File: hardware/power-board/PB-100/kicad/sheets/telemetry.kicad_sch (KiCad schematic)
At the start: 0 parts

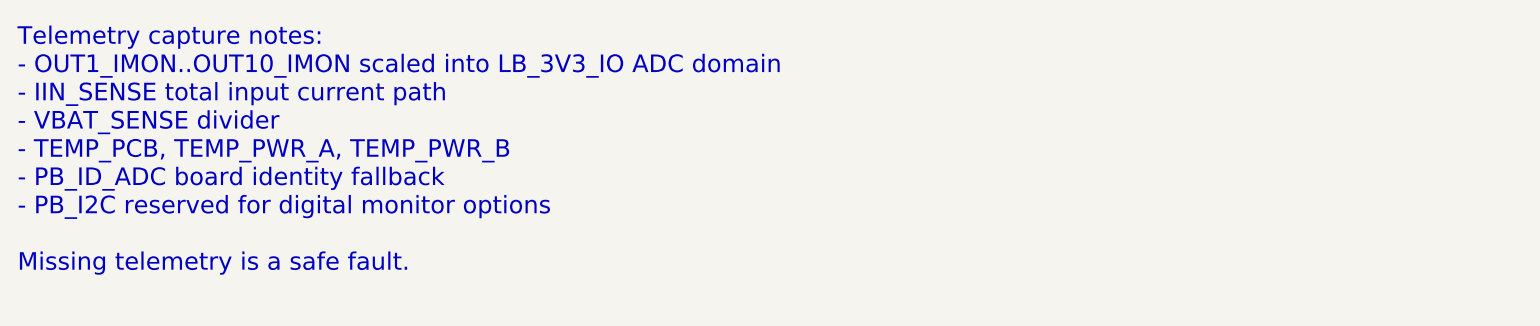
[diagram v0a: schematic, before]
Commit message: hardware: sync pb100 kicad sheet trace notes
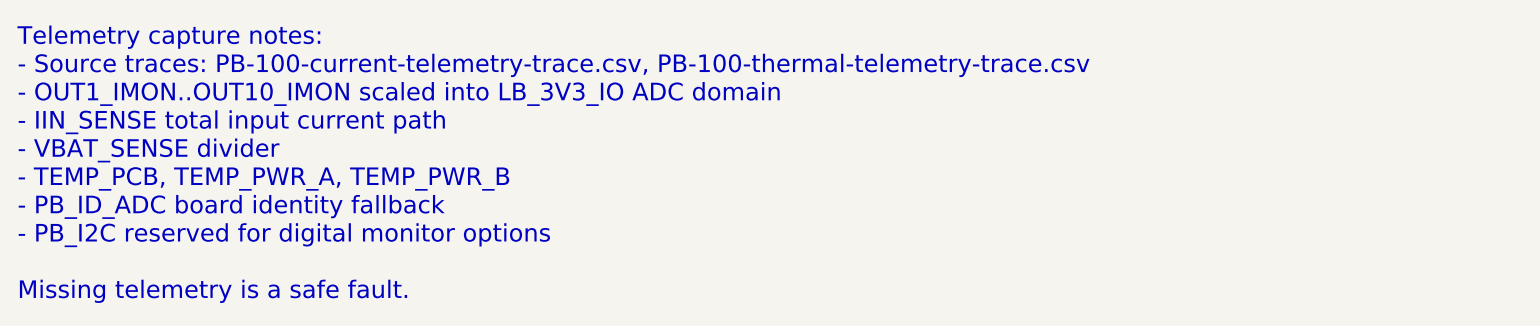
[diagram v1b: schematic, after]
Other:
- note added: "Telemetry capture notes: - Source traces: PB-100-current-telemetry-trace.csv, PB-100-thermal-telemetry-trace.csv - OUT1_IMON..OUT10_IMON scaled into LB_3V3_IO ADC domain - IIN_SENSE total input current path - VBAT_SENSE divider - TEMP_PCB, TEMP_PWR_A, TEMP_PWR_B - PB_ID_ADC board identity fallback - PB_I2C reserved for digital monitor options Missing telemetry is a safe fault."
- note removed: "Telemetry capture notes: - OUT1_IMON..OUT10_IMON scaled into LB_3V3_IO ADC domain - IIN_SENSE total input current path - VBAT_SENSE divider - TEMP_PCB, TEMP_PWR_A, TEMP_PWR_B - PB_ID_ADC board identity fallback - PB_I2C reserved for digital monitor options Missing telemetry is a safe fault."
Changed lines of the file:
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@@
     (comment 9 "Work queue: CAP-TEL. Telemetry capture follows current and thermal maps.")
     (comment 1 "Placeholder sheet. Capture current, voltage, thermal, and board ID telemetry here.")
-    (comment 2 "Sources: PB-100-current-telemetry.md and PB-100-thermal-telemetry.md.")
+    (comment 2 "Sources: PB-100-current-telemetry-trace.csv, PB-100-thermal-telemetry-trace.csv, telemetry maps.")
   )
-  (text "Telemetry capture notes:\n- OUT1_IMON..OUT10_IMON scaled into LB_3V3_IO ADC domain\n- IIN_SENSE total input current path\n- VBAT_SENSE divider\n- TEMP_PCB, TEMP_PWR_A, TEMP_PWR_B\n- PB_ID_ADC board identity fallback\n- PB_I2C reserved for digital monitor options\n\nMissing telemetry is a safe fault."
+  (text "Telemetry capture notes:\n- Source traces: PB-100-current-telemetry-trace.csv, PB-100-thermal-telemetry-trace.csv\n- OUT1_IMON..OUT10_IMON scaled into LB_3V3_IO ADC domain\n- IIN_SENSE total input current path\n- VBAT_SENSE divider\n- TEMP_PCB, TEMP_PWR_A, TEMP_PWR_B\n- PB_ID_ADC board identity fallback\n- PB_I2C reserved for digital monitor options\n\nMissing telemetry is a safe fault."
     (at 25 30 0)
     (effects (font (size 2.0 2.0)) (justify left top))

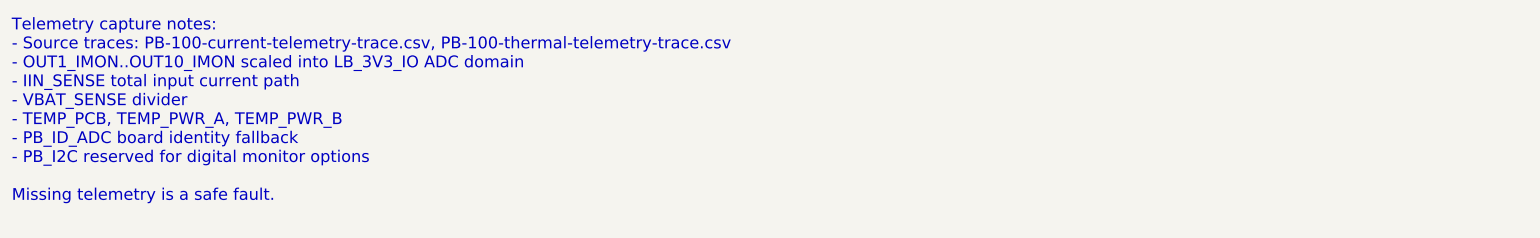
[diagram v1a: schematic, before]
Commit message: hardware: add pb100 current telemetry freeze review
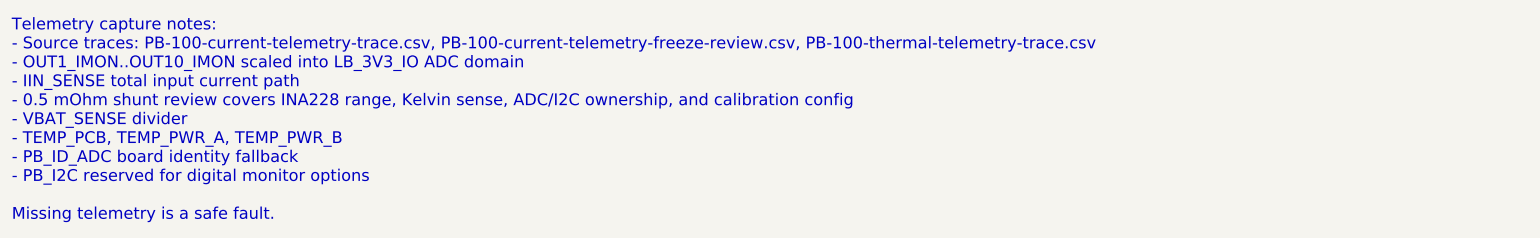
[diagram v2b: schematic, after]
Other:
- note added: "Telemetry capture notes: - Source traces: PB-100-current-telemetry-trace.csv, PB-100-current-telemetry-freeze-review.csv, PB-100-thermal-telemetry-trace.csv - OUT1_IMON..OUT10_IMON scaled into LB_3V3_IO ADC domain - IIN_SENSE total input current path - 0.5 mOhm shunt review covers INA228 range, Kelvin sense, ADC/I2C ownership, and calibration config - VBAT_SENSE divider - TEMP_PCB, TEMP_PWR_A, TE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"
- note removed: "Telemetry capture notes: - Source traces: PB-100-current-telemetry-trace.csv, PB-100-thermal-telemetry-trace.csv - OUT1_IMON..OUT10_IMON scaled into LB_3V3_IO ADC domain - IIN_SENSE total input current path - VBAT_SENSE divider - TEMP_PCB, TEMP_PWR_A, TEMP_PWR_B - PB_ID_ADC board identity fallback - PB_I2C reserved for digital monitor options Missing telemetry is a safe fault."
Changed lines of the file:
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@@
     (comment 9 "Work queue: CAP-TEL. Telemetry capture follows current and thermal maps.")
     (comment 1 "Placeholder sheet. Capture current, voltage, thermal, and board ID telemetry here.")
-    (comment 2 "Sources: PB-100-current-telemetry-trace.csv, PB-100-thermal-telemetry-trace.csv, telemetry maps.")
+    (comment 2 "Sources: PB-100-current-telemetry-trace.csv, PB-100-current-telemetry-freeze-review.csv, PB-100-thermal-telemetry-trace.csv, telemetry maps.")
   )
-  (text "Telemetry capture notes:\n- Source traces: PB-100-current-telemetry-trace.csv, PB-100-thermal-telemetry-trace.csv\n- OUT1_IMON..OUT10_IMON scaled into LB_3V3_IO ADC domain\n- IIN_SENSE total input current path\n- VBAT_SENSE divider\n- TEMP_PCB, TEMP_PWR_A, TEMP_PWR_B\n- PB_ID_ADC board identity fallback\n- PB_I2C reserved for digital monitor options\n\nMissing telemetry is a safe fault."
+  (text "Telemetry capture notes:\n- Source traces: PB-100-current-telemetry-trace.csv, PB-100-current-telemetry-freeze-review.csv, PB-100-thermal-telemetry-trace.csv\n- OUT1_IMON..OUT10_IMON scaled into LB_3V3_IO ADC domain\n- IIN_SENSE total input current path\n- 0.5 mOhm shunt review covers INA228 range, Kelvin sense, ADC/I2C ownership, and calibration config\n- VBAT_SENSE divider\n- TEMP_PCB, TEMP_PWR_A, TEMP_PWR_B\n- PB_ID_ADC board identity fallback\n- PB_I2C reserved for digital monitor options\n\nMissing telemetry is a safe fault."
     (at 25 30 0)
     (effects (font (size 2.0 2.0)) (justify left top))

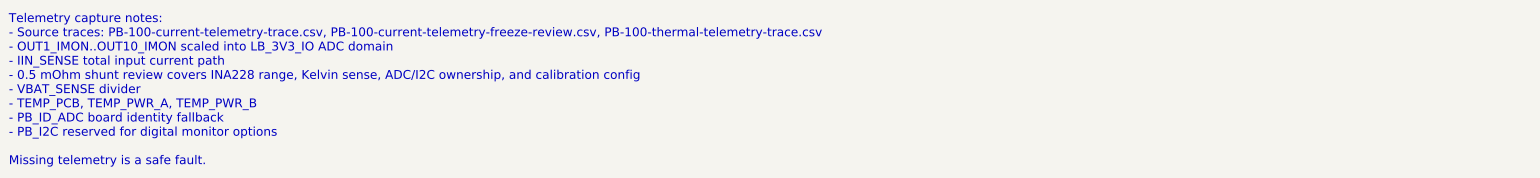
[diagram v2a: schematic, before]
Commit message: hardware: add pb100 thermal telemetry freeze review
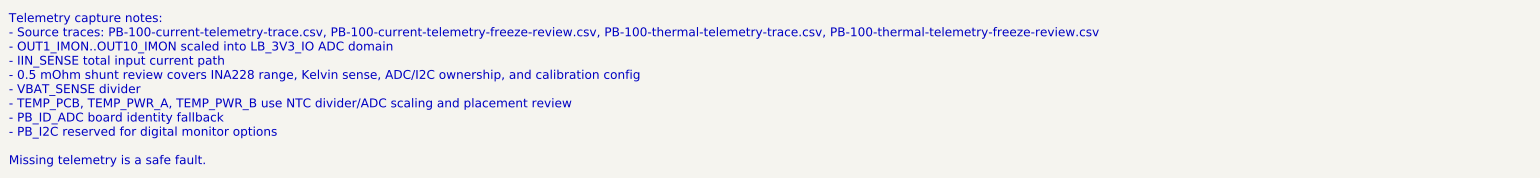
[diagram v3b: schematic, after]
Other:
- note added: "Telemetry capture notes: - Source traces: PB-100-current-telemetry-trace.csv, PB-100-current-telemetry-freeze-review.csv, PB-100-thermal-telemetry-trace.csv, PB-100-thermal-telemetry-freeze-review.csv - OUT1_IMON..OUT10_IMON scaled into LB_3V3_IO ADC domain - IIN_SENSE total input current path - 0.5 mOhm shunt review covers INA228 range, Kelvin sense, ADC/I2C ownership, and calibration config - V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"
- note removed: "Telemetry capture notes: - Source traces: PB-100-current-telemetry-trace.csv, PB-100-current-telemetry-freeze-review.csv, PB-100-thermal-telemetry-trace.csv - OUT1_IMON..OUT10_IMON scaled into LB_3V3_IO ADC domain - IIN_SENSE total input current path - 0.5 mOhm shunt review covers INA228 range, Kelvin sense, ADC/I2C ownership, and calibration config - VBAT_SENSE divider - TEMP_PCB, TEMP_PWR_A, TE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"
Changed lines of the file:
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@@
     (comment 9 "Work queue: CAP-TEL. Telemetry capture follows current and thermal maps.")
     (comment 1 "Placeholder sheet. Capture current, voltage, thermal, and board ID telemetry here.")
-    (comment 2 "Sources: PB-100-current-telemetry-trace.csv, PB-100-current-telemetry-freeze-review.csv, PB-100-thermal-telemetry-trace.csv, telemetry maps.")
+    (comment 2 "Sources: PB-100-current-telemetry-trace.csv, PB-100-current-telemetry-freeze-review.csv, PB-100-thermal-telemetry-trace.csv, PB-100-thermal-telemetry-freeze-review.csv, telemetry maps.")
   )
-  (text "Telemetry capture notes:\n- Source traces: PB-100-current-telemetry-trace.csv, PB-100-current-telemetry-freeze-review.csv, PB-100-thermal-telemetry-trace.csv\n- OUT1_IMON..OUT10_IMON scaled into LB_3V3_IO ADC domain\n- IIN_SENSE total input current path\n- 0.5 mOhm shunt review covers INA228 range, Kelvin sense, ADC/I2C ownership, and calibration config\n- VBAT_SENSE divider\n- TEMP_PCB, TEMP_PWR_A, TEMP_PWR_B\n- PB_ID_ADC board identity fallback\n- PB_I2C reserved for digital monitor options\n\nMissing telemetry is a safe fault."
+  (text "Telemetry capture notes:\n- Source traces: PB-100-current-telemetry-trace.csv, PB-100-current-telemetry-freeze-review.csv, PB-100-thermal-telemetry-trace.csv, PB-100-thermal-telemetry-freeze-review.csv\n- OUT1_IMON..OUT10_IMON scaled into LB_3V3_IO ADC domain\n- IIN_SENSE total input current path\n- 0.5 mOhm shunt review covers INA228 range, Kelvin sense, ADC/I2C ownership, and calibration config\n- VBAT_SENSE divider\n- TEMP_PCB, TEMP_PWR_A, TEMP_PWR_B use NTC divider/ADC scaling and placement review\n- PB_ID_ADC board identity fallback\n- PB_I2C reserved for digital monitor options\n\nMissing telemetry is a safe fault."
     (at 25 30 0)
     (effects (font (size 2.0 2.0)) (justify left top))

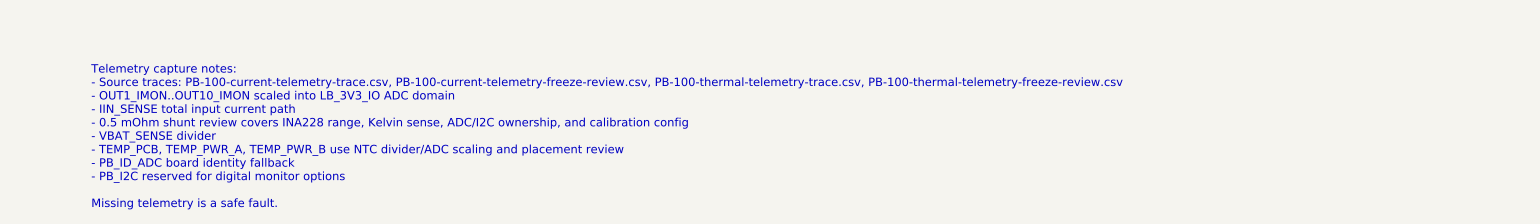
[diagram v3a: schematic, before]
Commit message: Capture preliminary PB-100 schematic sheets
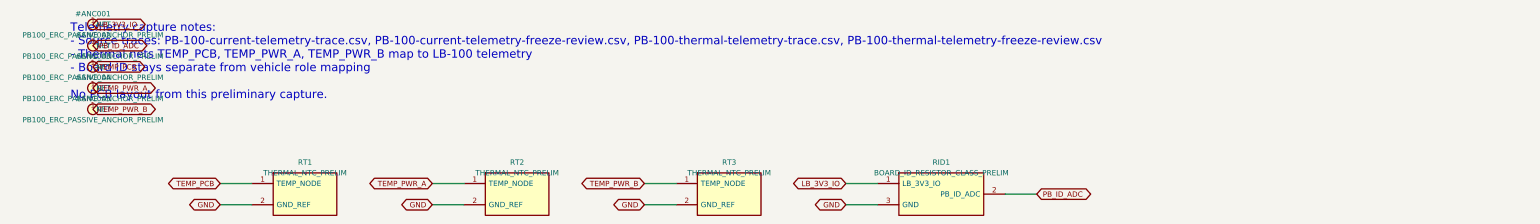
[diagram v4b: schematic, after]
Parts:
- added RID1: BOARD_ID_RESISTOR_CLASS_PRELIM, symbol PB100:PB100_BOARD_ID_RESISTOR_CLASS_PRELIM
- added RT1, RT2, RT3: THERMAL_NTC_PRELIM, symbol PB100:PB100_THERMAL_NTC_PRELIM
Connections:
- new net GND: RID1.3 (GND), RT1.2 (GND_REF), RT2.2 (GND_REF), RT3.2 (GND_REF)
- new net LB_3V3_IO: RID1.1 (LB_3V3_IO)
- new net PB_ID_ADC: RID1.2 (PB_ID_ADC)
- new net TEMP_PCB: RT1.1 (TEMP_NODE)
- new net TEMP_PWR_A: RT2.1 (TEMP_NODE)
- new net TEMP_PWR_B: RT3.1 (TEMP_NODE)
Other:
- note added: "Telemetry capture notes: - Source traces: PB-100-current-telemetry-trace.csv, PB-100-current-telemetry-freeze-review.csv, PB-100-thermal-telemetry-trace.csv, PB-100-thermal-telemetry-freeze-review.csv - Thermal nets TEMP_PCB, TEMP_PWR_A, TEMP_PWR_B map to LB-100 telemetry - Board ID stays separate from vehicle role mapping No PCB layout from this preliminary capture."
- note removed: "Telemetry capture notes: - Source traces: PB-100-current-telemetry-trace.csv, PB-100-current-telemetry-freeze-review.csv, PB-100-thermal-telemetry-trace.csv, PB-100-thermal-telemetry-freeze-review.csv - OUT1_IMON..OUT10_IMON scaled into LB_3V3_IO ADC domain - IIN_SENSE total input current path - 0.5 mOhm shunt review covers INA228 range, Kelvin sense, ADC/I2C ownership, and calibration config - V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"

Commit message: Add PB-100 current telemetry freeze checklist
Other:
- note added: "Telemetry capture notes: - Source traces: PB-100-current-telemetry-trace.csv, PB-100-current-telemetry-freeze-review.csv, PB-100-current-telemetry-value-freeze-checklist.csv, PB-100-thermal-telemetry-trace.csv, PB-100-thermal-telemetry-freeze-review.csv - Thermal nets TEMP_PCB, TEMP_PWR_A, TEMP_PWR_B map to LB-100 telemetry - Board ID stays separate from vehicle role mapping No PCB layout from th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"
- note removed: "Telemetry capture notes: - Source traces: PB-100-current-telemetry-trace.csv, PB-100-current-telemetry-freeze-review.csv, PB-100-thermal-telemetry-trace.csv, PB-100-thermal-telemetry-freeze-review.csv - Thermal nets TEMP_PCB, TEMP_PWR_A, TEMP_PWR_B map to LB-100 telemetry - Board ID stays separate from vehicle role mapping No PCB layout from this preliminary capture."
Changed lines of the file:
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@@
     (comment 9 "Work queue: CAP-TEL. Preliminary schematic capture follows PB-100-schematic-capture-work-queue.csv.")
     (comment 1 "Preliminary capture for current, voltage, thermal, and board ID telemetry.")
-    (comment 2 "Sources: PB-100-current-telemetry-trace.csv, PB-100-current-telemetry-freeze-review.csv, PB-100-thermal-telemetry-trace.csv, PB-100-thermal-telemetry-freeze-review.csv, telemetry maps.")
+    (comment 2 "Sources: PB-100-current-telemetry-trace.csv, PB-100-current-telemetry-freeze-review.csv, PB-100-current-telemetry-value-freeze-checklist.csv, PB-100-thermal-telemetry-trace.csv, PB-100-thermal-telemetry-freeze-review.csv, telemetry maps.")
   )
-  (text "Telemetry capture notes:\n- Source traces: PB-100-current-telemetry-trace.csv, PB-100-current-telemetry-freeze-review.csv, PB-100-thermal-telemetry-trace.csv, PB-100-thermal-telemetry-freeze-review.csv\n- Thermal nets TEMP_PCB, TEMP_PWR_A, TEMP_PWR_B map to LB-100 telemetry\n- Board ID stays separate from vehicle role mapping\n\nNo PCB layout from this preliminary capture."
+  (text "Telemetry capture notes:\n- Source traces: PB-100-current-telemetry-trace.csv, PB-100-current-telemetry-freeze-review.csv, PB-100-current-telemetry-value-freeze-checklist.csv, PB-100-thermal-telemetry-trace.csv, PB-100-thermal-telemetry-freeze-review.csv\n- Thermal nets TEMP_PCB, TEMP_PWR_A, TEMP_PWR_B map to LB-100 telemetry\n- Board ID stays separate from vehicle role mapping\n\nNo PCB layout from this preliminary capture."
     (at 20 20 0)
     (effects (font (size 2.0 2.0)) (justify left top))
